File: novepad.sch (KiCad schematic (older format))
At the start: 4 parts, among them J101 NOVENA_LCD_CONN, J102 LP097QX1_CONN

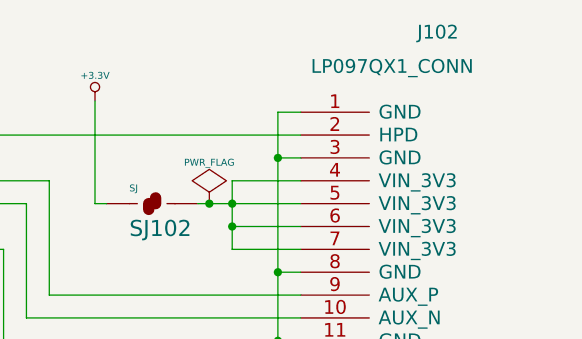
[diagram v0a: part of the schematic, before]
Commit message: Swap fault/slow start FET for inrush current limiting thermistor
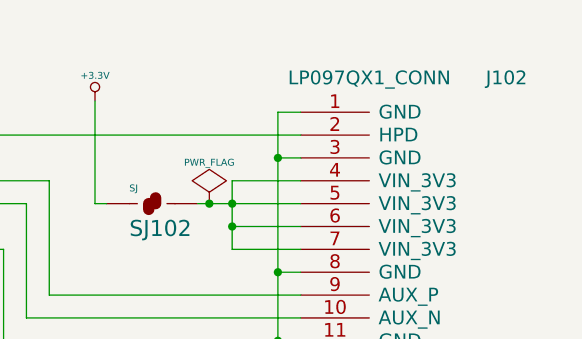
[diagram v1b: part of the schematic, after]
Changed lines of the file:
@@
 U 1 1 543B8313
 P 10350 2050
-F 0 "J102" H 10550 3700 60  0000 C CNN
-F 1 "LP097QX1_CONN" H 10350 3550 60  0000 C CNN
+F 0 "J102" H 10850 3500 60  0000 C CNN
+F 1 "LP097QX1_CONN" H 10250 3500 60  0000 C CNN
 F 2 "" H 10350 2050 60  0000 C CNN
 F 3 "" H 10350 2050 60  0000 C CNN

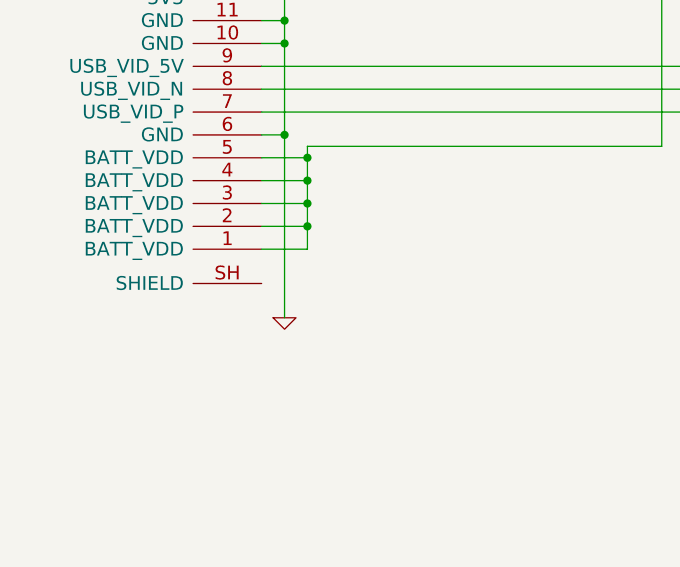
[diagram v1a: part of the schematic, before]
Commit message: Add shield pin to Novena LCD connector
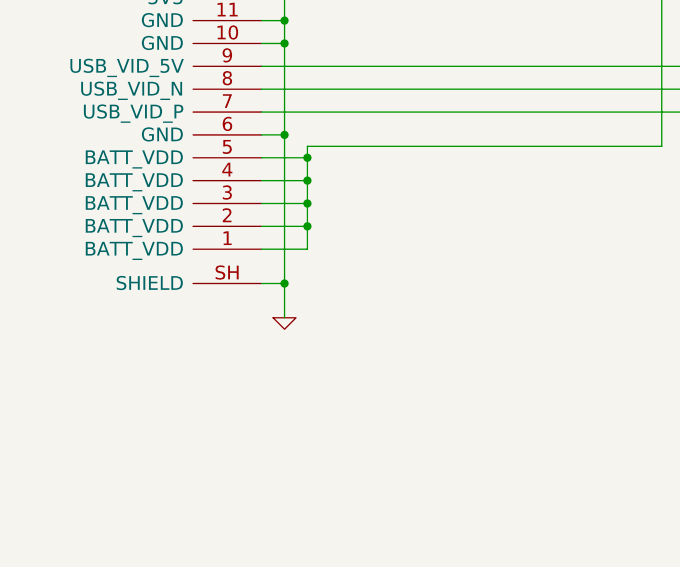
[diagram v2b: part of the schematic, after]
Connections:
- wire segments 181 -> 182
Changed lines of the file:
@@
 	9050 1150 9100 1150
 Connection ~ 9550 1150
+Wire Wire Line
+	2100 6300 2200 6300
+Connection ~ 2200 6300
 $EndSCHEMATC

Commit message: Initial footprint association, last few footprints
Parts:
- J101: footprint (none) -> novepad:MOLEX_502250_8051
- J102: footprint (none) -> novepad:MOLEX_51926_5494
- SJ101, SJ102: footprint (none) -> FT:SJ_SHORTED
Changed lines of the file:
@@
 LIBS:valves
 LIBS:novepad-cache
-EELAYER 24 0
+EELAYER 25 0
 EELAYER END
 $Descr A4 11693 8268
@@
 F 0 "J102" H 10850 3500 60  0000 C CNN
 F 1 "LP097QX1_CONN" H 10250 3500 60  0000 C CNN
-F 2 "" H 10350 2050 60  0000 C CNN
+F 2 "novepad:MOLEX_51926_5494" H 10350 2050 60  0001 C CNN
 F 3 "" H 10350 2050 60  0000 C CNN
 	1    10350 2050
@@
 F 0 "J101" H 2050 6450 60  0000 C CNN
 F 1 "NOVENA_LCD_CONN" H 1700 6350 60  0000 C CNN
-F 2 "" H 2800 4650 60  0000 C CNN
+F 2 "novepad:MOLEX_502250_8051" H 2800 4650 60  0001 C CNN
 F 3 "" H 2800 4650 60  0000 C CNN
 	1    1650 3500
@@
 F 0 "SJ102" H 9200 1000 70  0000 L BNN
 F 1 "SJ" H 9200 1200 30  0000 L BNN
-F 2 "" H 9300 1150 60  0000 C CNN
+F 2 "FT:SJ_SHORTED" H 9300 1150 60  0001 C CNN
 F 3 "" H 9300 1150 60  0000 C CNN
 	1    9300 1150
@@
 F 0 "SJ101" H 2500 4700 70  0000 L BNN
 F 1 "SJ" H 2500 4900 30  0000 L BNN
-F 2 "" H 2600 4850 60  0000 C CNN
+F 2 "FT:SJ_SHORTED" H 2600 4850 60  0001 C CNN
 F 3 "" H 2600 4850 60  0000 C CNN
 	1    2600 4850

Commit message: First attempt at routing the high speed differential traces
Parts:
- J101: footprint novepad:MOLEX_502250_8051 -> novepad:MOLEX_51926_5494
- J102: footprint novepad:MOLEX_51926_5494 -> novepad:MOLEX_502250_8051
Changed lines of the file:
@@
 F 0 "J102" H 10850 3500 60  0000 C CNN
 F 1 "LP097QX1_CONN" H 10250 3500 60  0000 C CNN
-F 2 "novepad:MOLEX_51926_5494" H 10350 2050 60  0001 C CNN
+F 2 "novepad:MOLEX_502250_8051" H 10350 2050 60  0001 C CNN
 F 3 "" H 10350 2050 60  0000 C CNN
 	1    10350 2050
@@
 F 0 "J101" H 2050 6450 60  0000 C CNN
 F 1 "NOVENA_LCD_CONN" H 1700 6350 60  0000 C CNN
-F 2 "novepad:MOLEX_502250_8051" H 2800 4650 60  0001 C CNN
+F 2 "novepad:MOLEX_51926_5494" H 2800 4650 60  0001 C CNN
 F 3 "" H 2800 4650 60  0000 C CNN
 	1    1650 3500
